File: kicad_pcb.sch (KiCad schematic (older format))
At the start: 162 parts, among them J1 USB_B_Mini, SW1 SW_Push, U1 ATmega32U4-AU, Y1 16Mhz

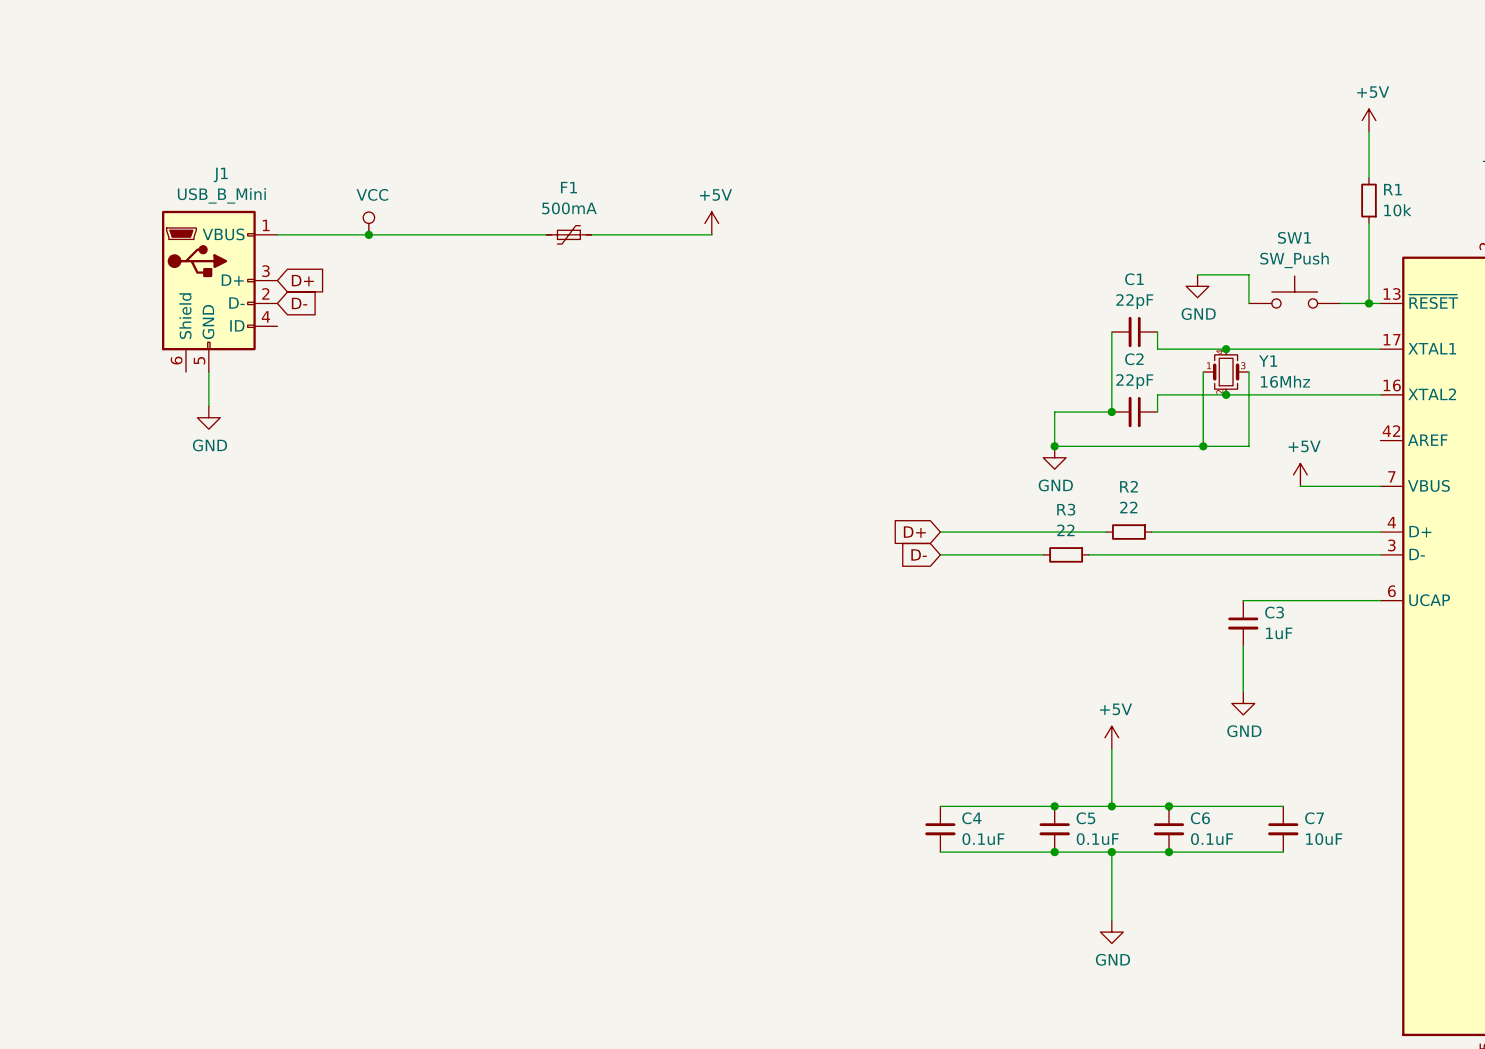
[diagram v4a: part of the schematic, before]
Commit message: Moved and re-routed traces for C7 decoupling capacitor
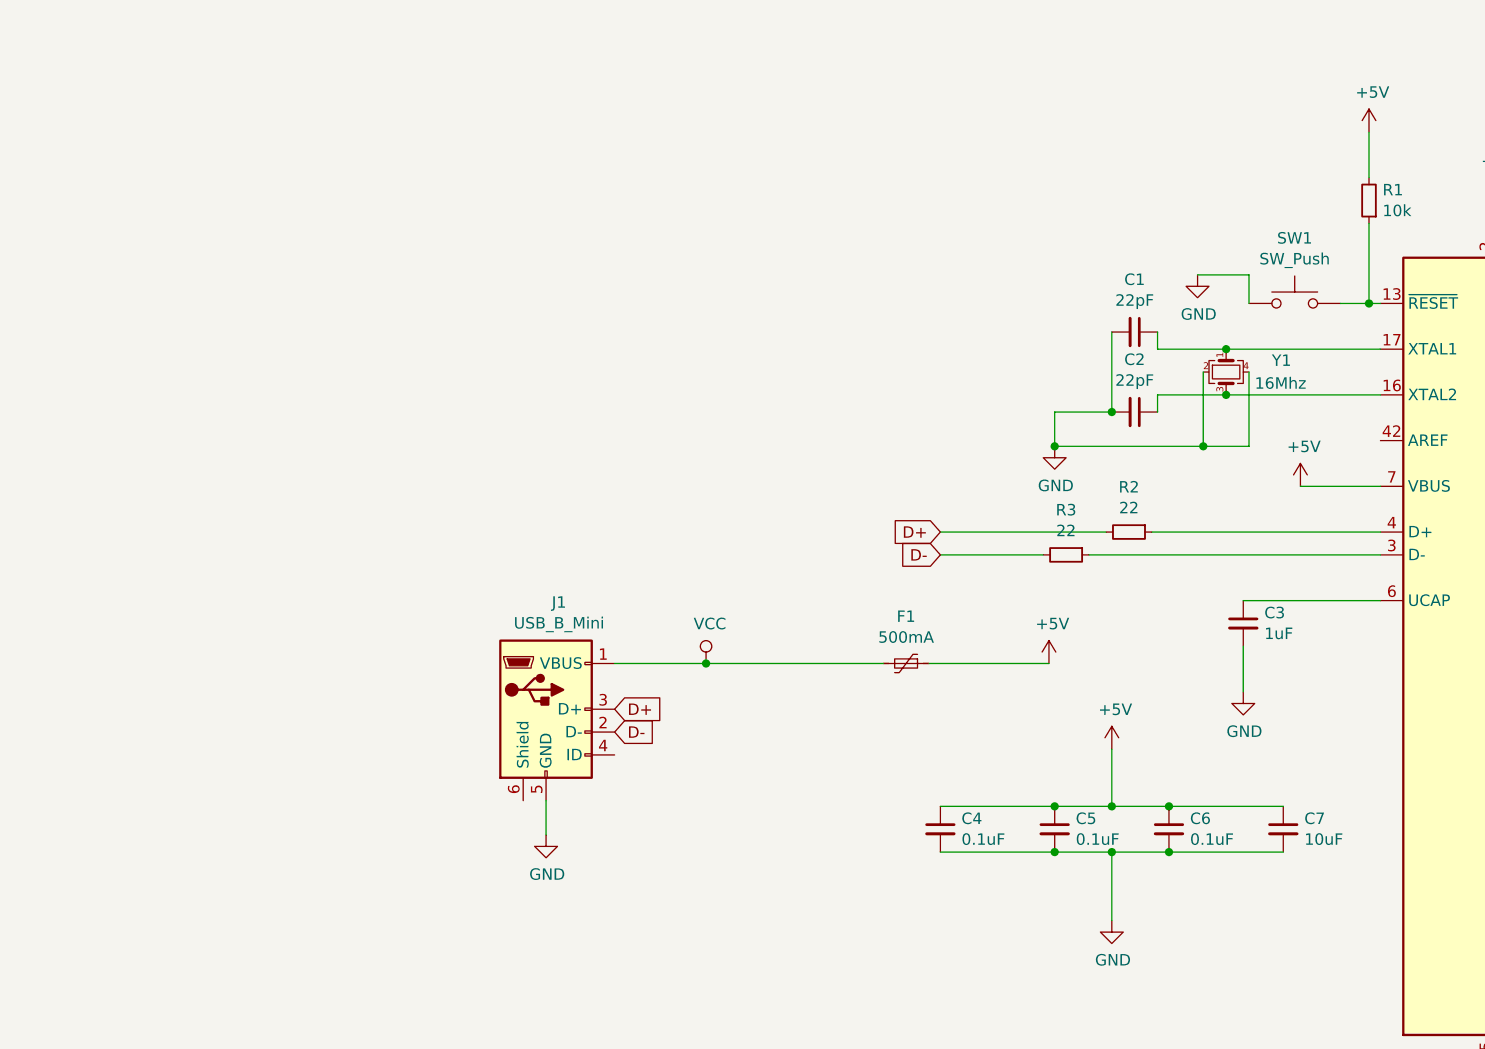
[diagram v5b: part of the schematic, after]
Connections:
- net GND: now also Y1.2, Y1.4; no longer Y1.1, Y1.3
- net at C2.1, U1.16 (XTAL2): now also Y1.3; no longer Y1.2
- net at C1.1, U1.17 (XTAL1): now also Y1.1; no longer Y1.4
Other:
- moved on the sheet: F1, J1
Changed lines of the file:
@@
 Connection ~ 6750 12500
-Wire Wire Line
-	6750 12500 7000 12500
-Connection ~ 7250 12500
-Wire Wire Line
-	7250 12500 7750 12500
 Wire Wire Line
 	7750 12700 7250 12700
@@
 Wire Wire Line
 	8175 11100 7825 11100
-$Comp
-L Device:Crystal_GND24_Small Y1
-U 1 1 5CCBDFE5
-P 7500 10600
-F 0 "Y1" H 7644 10646 50  0000 L CNN
-F 1 "16Mhz" H 7644 10555 50  0000 L CNN
-F 2 "Crystal:Crystal_SMD_3225-4Pin_3.2x2.5mm" H 7500 10600 50  0001 C CNN
-F 3 "~" H 7500 10600 50  0001 C CNN
-	1    7500 10600
-	1    0    0    -1
-$EndComp
-Wire Wire Line
-	8175 10700 7500 10700
-Wire Wire Line
-	8175 10500 7500 10500
 $Comp
 L Device:C_Small C1
@@
 $EndComp
 Wire Wire Line
-	7400 10600 7400 10925
-Wire Wire Line
 	7400 10925 6750 10925
-Wire Wire Line
-	7600 10600 7600 10925
 Wire Wire Line
 	7600 10925 7400 10925
 Connection ~ 7400 10925
 Wire Wire Line
-	7500 10700 7200 10700
-Wire Wire Line
 	7200 10700 7200 10775
-Connection ~ 7500 10700
-Wire Wire Line
-	7500 10500 7200 10500
 Wire Wire Line
 	7200 10500 7200 10425
-Connection ~ 7500 10500
 Wire Wire Line
 	7000 10425 7000 10775
@@
 L Connector:USB_B_Mini J1
 U 1 1 5CCDCA3B
-P 3050 10200
-F 0 "J1" H 3107 10667 50  0000 C CNN
-F 1 "USB_B_Mini" H 3107 10576 50  0000 C CNN
-F 2 "random-keyboard-parts:Molex-0548190589" H 3200 10150 50  0001 C CNN
-F 3 "~" H 3200 10150 50  0001 C CNN
-	1    3050 10200
+P 4525 12075
+F 0 "J1" H 4582 12542 50  0000 C CNN
+F 1 "USB_B_Mini" H 4582 12451 50  0000 C CNN
+F 2 "random-keyboard-parts:Molex-0548190589" H 4675 12025 50  0001 C CNN
+F 3 "~" H 4675 12025 50  0001 C CNN
+	1    4525 12075
 	1    0    0    -1
 $EndComp
@@
 L Device:Polyfuse_Small F1
 U 1 1 5CCDD8D1
-P 4625 10000
-F 0 "F1" V 4420 10000 50  0000 C CNN
-F 1 "500mA" V 4511 10000 50  0000 C CNN
-F 2 "Fuse:Fuse_1206_3216Metric" H 4675 9800 50  0001 L CNN
-F 3 "~" H 4625 10000 50  0001 C CNN
-	1    4625 10000
+P 6100 11875
+F 0 "F1" V 5895 11875 50  0000 C CNN
+F 1 "500mA" V 5986 11875 50  0000 C CNN
+F 2 "Fuse:Fuse_1206_3216Metric" H 6150 11675 50  0001 L CNN
+F 3 "~" H 6100 11875 50  0001 C CNN
+	1    6100 11875
 	0    1    1    0
 $EndComp
@@
 L power:+5V #PWR0111
 U 1 1 5CCDE608
-P 5250 10000
-F 0 "#PWR0111" H 5250 9850 50  0001 C CNN
-F 1 "+5V" H 5265 10173 50  0000 C CNN
-F 2 "" H 5250 10000 50  0001 C CNN
-F 3 "" H 5250 10000 50  0001 C CNN
-	1    5250 10000
+P 6725 11875
+F 0 "#PWR0111" H 6725 11725 50  0001 C CNN
+F 1 "+5V" H 6740 12048 50  0000 C CNN
+F 2 "" H 6725 11875 50  0001 C CNN
+F 3 "" H 6725 11875 50  0001 C CNN
+	1    6725 11875
 	1    0    0    -1
 $EndComp
@@
 L power:VCC #PWR0112
 U 1 1 5CCDEDD0
-P 3750 10000
-F 0 "#PWR0112" H 3750 9850 50  0001 C CNN
-F 1 "VCC" H 3767 10173 50  0000 C CNN
-F 2 "" H 3750 10000 50  0001 C CNN
-F 3 "" H 3750 10000 50  0001 C CNN
-	1    3750 10000
-	1    0    0    -1
-$EndComp
-Wire Wire Line
-	3350 10000 3750 10000
-Connection ~ 3750 10000
-Wire Wire Line
-	3750 10000 4525 10000
-Wire Wire Line
-	4725 10000 5250 10000
-Text GLabel 3350 10200 2    50   Input ~ 0
+P 5225 11875
+F 0 "#PWR0112" H 5225 11725 50  0001 C CNN
+F 1 "VCC" H 5242 12048 50  0000 C CNN
+F 2 "" H 5225 11875 50  0001 C CNN
+F 3 "" H 5225 11875 50  0001 C CNN
+	1    5225 11875
+	1    0    0    -1
+$EndComp
+Wire Wire Line
+	4825 11875 5225 11875
+Connection ~ 5225 11875
+Wire Wire Line
+	5225 11875 6000 11875
+Wire Wire Line
+	6200 11875 6725 11875
+Text GLabel 4825 12075 2    50   Input ~ 0
 D+
-Text GLabel 3350 10300 2    50   Input ~ 0
+Text GLabel 4825 12175 2    50   Input ~ 0
 D-
 $Comp
 L power:GND #PWR0113
 U 1 1 5CCE29A1
-P 3050 10750
-F 0 "#PWR0113" H 3050 10500 50  0001 C CNN
-F 1 "GND" H 3055 10577 50  0000 C CNN
-F 2 "" H 3050 10750 50  0001 C CNN
-F 3 "" H 3050 10750 50  0001 C CNN
-	1    3050 10750
-	1    0    0    -1
-$EndComp
-Wire Wire Line
-	3050 10600 3050 10750
+P 4525 12625
+F 0 "#PWR0113" H 4525 12375 50  0001 C CNN
+F 1 "GND" H 4530 12452 50  0000 C CNN
+F 2 "" H 4525 12625 50  0001 C CNN
+F 3 "" H 4525 12625 50  0001 C CNN
+	1    4525 12625
+	1    0    0    -1
+$EndComp
+Wire Wire Line
+	4525 12475 4525 12625
 Wire Wire Line
 	7500 5050 7500 6050
@@
 Text GLabel 9475 11500 2    50   Input ~ 0
 ROW1
+Wire Wire Line
+	6750 12500 7000 12500
+Connection ~ 7250 12500
+Wire Wire Line
+	7250 12500 7750 12500
+Connection ~ 7500 10500
+Wire Wire Line
+	7500 10500 7200 10500
+Wire Wire Line
+	8175 10500 7500 10500
+Wire Wire Line
+	7600 10600 7600 10925
+Connection ~ 7500 10700
+Wire Wire Line
+	7500 10700 7200 10700
+Wire Wire Line
+	8175 10700 7500 10700
+Wire Wire Line
+	7400 10600 7400 10925
+$Comp
+L Device:Crystal_GND24_Small Y1
+U 1 1 5CCBDFE5
+P 7500 10600
+F 0 "Y1" V 7450 10800 50  0000 L CNN
+F 1 "16Mhz" V 7550 10725 50  0000 L CNN
+F 2 "Crystal:Crystal_SMD_3225-4Pin_3.2x2.5mm" H 7500 10600 50  0001 C CNN
+F 3 "~" H 7500 10600 50  0001 C CNN
+	1    7500 10600
+	0    1    1    0
+$EndComp
 $EndSCHEMATC

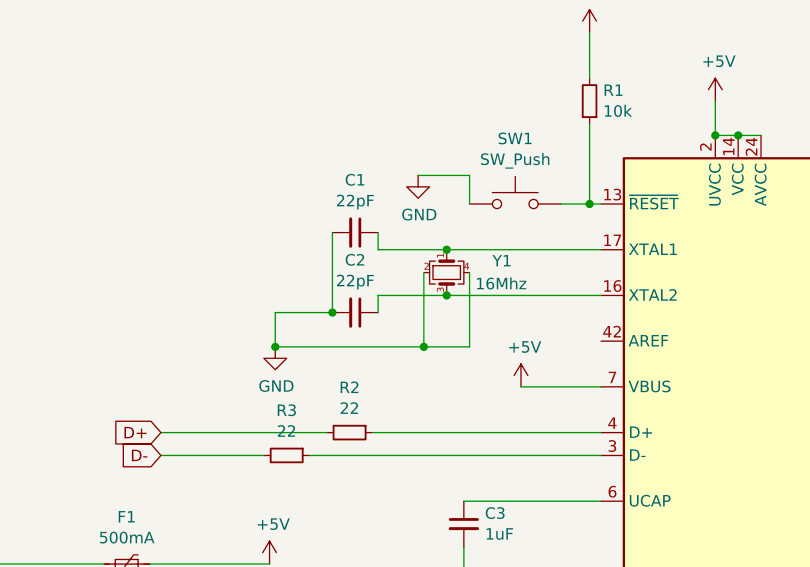
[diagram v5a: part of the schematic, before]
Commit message: started to restructure the routing
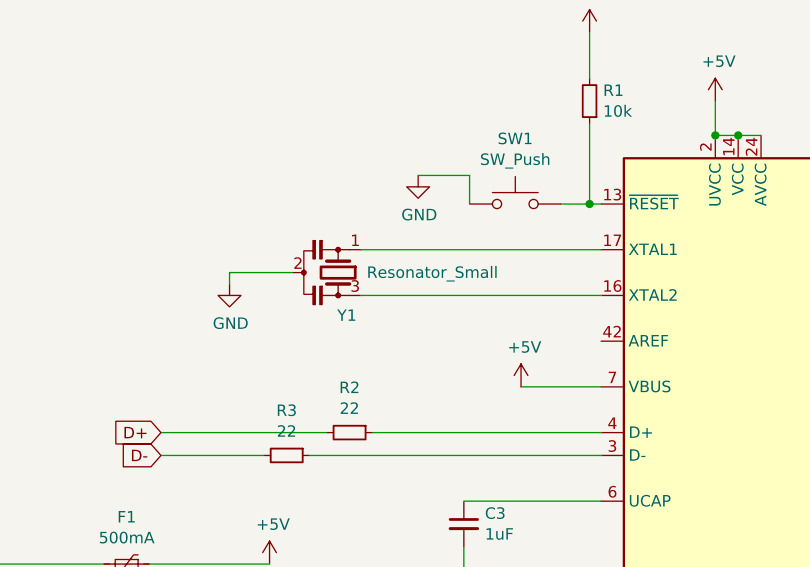
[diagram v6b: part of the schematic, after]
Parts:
- removed C1, C2: 22pF, Capacitor_SMD:C_0805_2012Metric, symbol Device:C_Small
- removed Y1: 16Mhz, Crystal:Crystal_SMD_3225-4Pin_3.2x2.5mm, symbol Device:Crystal_GND24_Small
- added Y1: Resonator_Small, Crystal:Resonator_SMD_muRata_CSTxExxV-3Pin_3.0x1.1mm, symbol Device:Resonator_Small
- J1: footprint random-keyboard-parts:Molex-0548190589 -> random-keyboard-parts:Molex-0548190519
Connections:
- net GND: now also Y1.2
- net at U1.16 (XTAL2): now also Y1.3
- net at U1.17 (XTAL1): now also Y1.1
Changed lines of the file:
@@
 	8175 11100 7825 11100
-$Comp
-L Device:C_Small C1
-U 1 1 5CCC2436
-P 7100 10425
-F 0 "C1" V 6871 10425 50  0000 C CNN
-F 1 "22pF" V 6962 10425 50  0000 C CNN
-F 2 "Capacitor_SMD:C_0805_2012Metric" H 7100 10425 50  0001 C CNN
-F 3 "~" H 7100 10425 50  0001 C CNN
-	1    7100 10425
-	0    1    1    0
-$EndComp
-$Comp
-L Device:C_Small C2
-U 1 1 5CCC3005
-P 7100 10775
-F 0 "C2" V 6871 10775 50  0000 C CNN
-F 1 "22pF" V 6962 10775 50  0000 C CNN
-F 2 "Capacitor_SMD:C_0805_2012Metric" H 7100 10775 50  0001 C CNN
-F 3 "~" H 7100 10775 50  0001 C CNN
-	1    7100 10775
-	0    1    1    0
-$EndComp
-$Comp
-L power:GND #PWR0108
-U 1 1 5CCC33BA
-P 6750 10925
-F 0 "#PWR0108" H 6750 10675 50  0001 C CNN
-F 1 "GND" H 6755 10752 50  0000 C CNN
-F 2 "" H 6750 10925 50  0001 C CNN
-F 3 "" H 6750 10925 50  0001 C CNN
-	1    6750 10925
-	1    0    0    -1
-$EndComp
-Wire Wire Line
-	7400 10925 6750 10925
-Wire Wire Line
-	7600 10925 7400 10925
-Connection ~ 7400 10925
-Wire Wire Line
-	7200 10700 7200 10775
-Wire Wire Line
-	7200 10500 7200 10425
-Wire Wire Line
-	7000 10425 7000 10775
-Wire Wire Line
-	7000 10775 6750 10775
-Wire Wire Line
-	6750 10775 6750 10925
-Connection ~ 7000 10775
-Connection ~ 6750 10925
 $Comp
 L Switch:SW_Push SW1
@@
 F 0 "J1" H 4582 12542 50  0000 C CNN
 F 1 "USB_B_Mini" H 4582 12451 50  0000 C CNN
-F 2 "random-keyboard-parts:Molex-0548190589" H 4675 12025 50  0001 C CNN
+F 2 "random-keyboard-parts:Molex-0548190519" H 4675 12025 50  0001 C CNN
 F 3 "~" H 4675 12025 50  0001 C CNN
 	1    4525 12075
@@
 Wire Wire Line
 	7250 12500 7750 12500
-Connection ~ 7500 10500
-Wire Wire Line
-	7500 10500 7200 10500
-Wire Wire Line
-	8175 10500 7500 10500
-Wire Wire Line
-	7600 10600 7600 10925
-Connection ~ 7500 10700
-Wire Wire Line
-	7500 10700 7200 10700
-Wire Wire Line
-	8175 10700 7500 10700
-Wire Wire Line
-	7400 10600 7400 10925
-$Comp
-L Device:Crystal_GND24_Small Y1
-U 1 1 5CCBDFE5
-P 7500 10600
-F 0 "Y1" V 7450 10800 50  0000 L CNN
-F 1 "16Mhz" V 7550 10725 50  0000 L CNN
-F 2 "Crystal:Crystal_SMD_3225-4Pin_3.2x2.5mm" H 7500 10600 50  0001 C CNN
-F 3 "~" H 7500 10600 50  0001 C CNN
-	1    7500 10600
+$Comp
+L Device:Resonator_Small Y1
+U 1 1 5D4D1439
+P 7025 10600
+F 0 "Y1" V 7213 10596 50  0000 L CNN
+F 1 "Resonator_Small" V 7025 10725 50  0000 L CNN
+F 2 "Crystal:Resonator_SMD_muRata_CSTxExxV-3Pin_3.0x1.1mm" H 7000 10600 50  0001 C CNN
+F 3 "~" H 7000 10600 50  0001 C CNN
+	1    7025 10600
 	0    1    1    0
 $EndComp
+$Comp
+L power:GND #PWR0108
+U 1 1 5CCC33BA
+P 6550 10650
+F 0 "#PWR0108" H 6550 10400 50  0001 C CNN
+F 1 "GND" H 6555 10477 50  0000 C CNN
+F 2 "" H 6550 10650 50  0001 C CNN
+F 3 "" H 6550 10650 50  0001 C CNN
+	1    6550 10650
+	1    0    0    -1
+$EndComp
+Wire Wire Line
+	8175 10500 7125 10500
+Wire Wire Line
+	7125 10700 8175 10700
+Wire Wire Line
+	6825 10600 6550 10600
+Wire Wire Line
+	6550 10600 6550 10650
 $EndSCHEMATC

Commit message: further routing
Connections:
- net COL0: now also U1.41 (PF0); no longer U1.1 (PE6)
- net COL1: now also U1.40 (PF1); no longer U1.41 (PF0)
- net COL10: now also U1.28 (PB4); no longer U1.25 (PD4)
- net COL11: now also U1.21 (PD3); no longer U1.22 (PD5)
- net COL12: now also U1.20 (PD2); no longer U1.21 (PD3)
- net COL13: now also U1.19 (PD1); no longer U1.20 (PD2)
- net COL14: now also U1.18 (PD0); no longer U1.19 (PD1)
- net COL2: now also U1.39 (PF4); no longer U1.40 (PF1)
- net COL3: now also U1.38 (PF5); no longer U1.39 (PF4)
- net COL6: now also U1.32 (PC7); no longer U1.38 (PF5)
- net COL8: now also U1.30 (PB6); no longer U1.28 (PB4)
- net COL9: now also U1.29 (PB5); no longer U1.26 (PD6)
- net ROW1: now also U1.1 (PE6); no longer U1.18 (PD0)
- net ROW2: now also U1.22 (PD5); no longer U1.29 (PB5)
- net ROW3: now also U1.25 (PD4); no longer U1.12 (PB7)
- net ROW4: now also U1.26 (PD6); no longer U1.30 (PB6)
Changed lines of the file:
@@
 	5000 5050 5000 6050
 Connection ~ 5000 5050
-Text GLabel 9475 10800 2    50   Input ~ 0
+Text GLabel 9475 12000 2    50   Input ~ 0
 ROW2
 Text GLabel 9475 10300 2    50   Input ~ 0
 ROW0
-Text GLabel 9475 11800 2    50   Input ~ 0
+Text GLabel 9475 11700 2    50   Input ~ 0
 COL12
-Text GLabel 9475 11700 2    50   Input ~ 0
+Text GLabel 9475 11600 2    50   Input ~ 0
 COL13
-Text GLabel 9475 11900 2    50   Input ~ 0
+Text GLabel 9475 10700 2    50   Input ~ 0
 COL10
 Text GLabel 9475 13100 2    50   Input ~ 0
@@
 Text GLabel 9475 13200 2    50   Input ~ 0
 COL5
+Text GLabel 9475 13000 2    50   Input ~ 0
+COL3
 Text GLabel 9475 12900 2    50   Input ~ 0
-COL3
-Text GLabel 9475 12500 2    50   Input ~ 0
-COL0
+COL2
 Text GLabel 9475 12800 2    50   Input ~ 0
-COL2
-Text GLabel 9475 12700 2    50   Input ~ 0
 COL1
 Connection ~ 8675 13600
@@
 	1    0    0    -1
 $EndComp
-Text GLabel 9475 11600 2    50   Input ~ 0
+Text GLabel 9475 11500 2    50   Input ~ 0
 COL14
 Wire Wire Line
@@
 Wire Wire Line
 	9475 11600 9375 11600
-Text GLabel 9475 13000 2    50   Input ~ 0
+Text GLabel 9475 11300 2    50   Input ~ 0
 COL6
-Text GLabel 9475 10700 2    50   Input ~ 0
+Text GLabel 9475 10900 2    50   Input ~ 0
 COL8
 Wire Wire Line
@@
 Wire Wire Line
 	9475 13200 9375 13200
-Text GLabel 9475 10900 2    50   Input ~ 0
+Text GLabel 9475 12100 2    50   Input ~ 0
 ROW4
-Text GLabel 9475 11000 2    50   Input ~ 0
+Text GLabel 9475 11900 2    50   Input ~ 0
 ROW3
-Text GLabel 9475 12100 2    50   Input ~ 0
+Text GLabel 9475 10800 2    50   Input ~ 0
 COL9
-Text GLabel 9475 12000 2    50   Input ~ 0
+Text GLabel 9475 11800 2    50   Input ~ 0
 COL11
 Text GLabel 9475 11200 2    50   Input ~ 0
 COL7
-Text GLabel 9475 11500 2    50   Input ~ 0
+Text GLabel 9475 12500 2    50   Input ~ 0
 ROW1
 Wire Wire Line
@@
 Wire Wire Line
 	6550 10600 6550 10650
+Text GLabel 9475 12700 2    50   Input ~ 0
+COL0
 $EndSCHEMATC

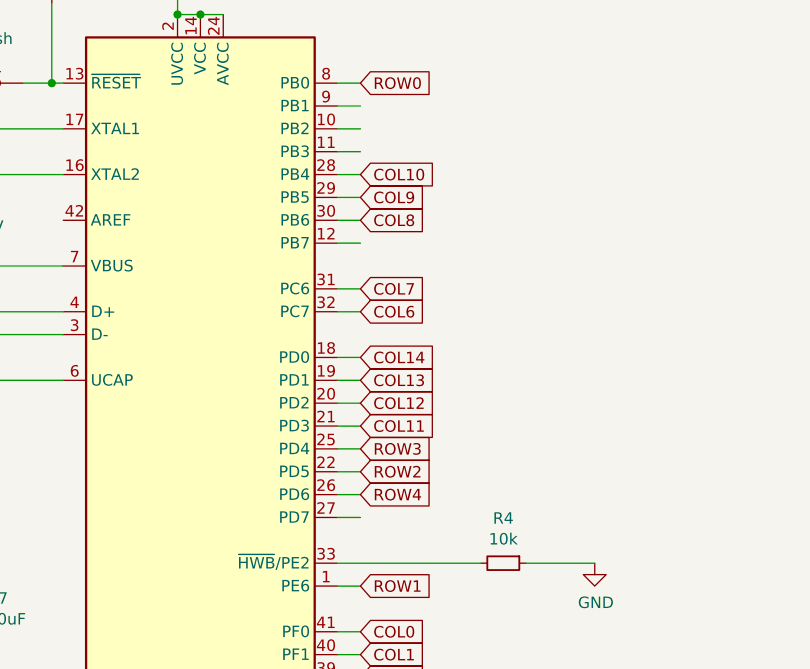
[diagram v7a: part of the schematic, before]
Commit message: finished all routing, except the bottom row
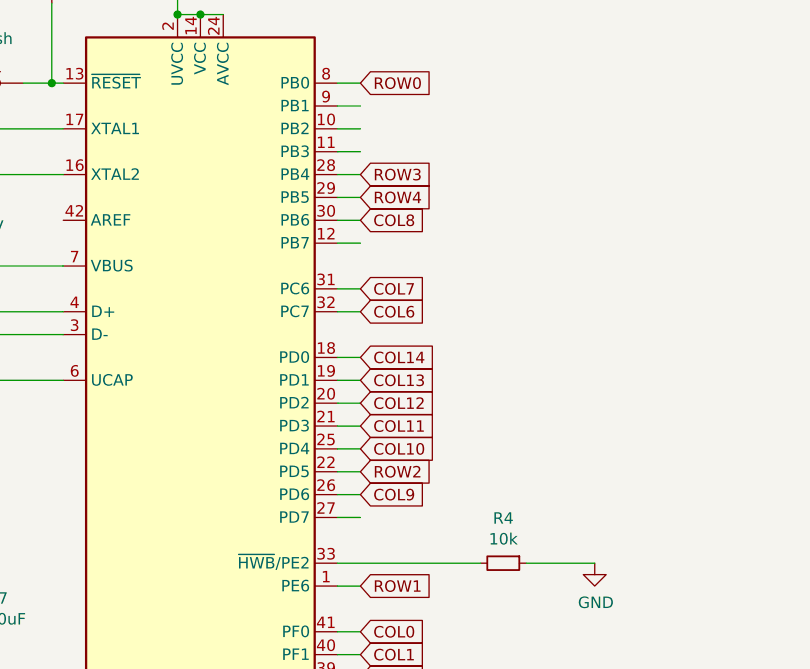
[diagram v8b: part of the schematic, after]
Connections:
- net COL10: now also U1.25 (PD4); no longer U1.28 (PB4)
- net COL9: now also U1.26 (PD6); no longer U1.29 (PB5)
- net ROW3: now also U1.28 (PB4); no longer U1.25 (PD4)
- net ROW4: now also U1.29 (PB5); no longer U1.26 (PD6)
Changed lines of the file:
@@
 Text GLabel 9475 11600 2    50   Input ~ 0
 COL13
-Text GLabel 9475 10700 2    50   Input ~ 0
+Text GLabel 9475 11900 2    50   Input ~ 0
 COL10
 Text GLabel 9475 13100 2    50   Input ~ 0
@@
 Wire Wire Line
 	9475 13200 9375 13200
+Text GLabel 9475 10800 2    50   Input ~ 0
+ROW4
+Text GLabel 9475 10700 2    50   Input ~ 0
+ROW3
 Text GLabel 9475 12100 2    50   Input ~ 0
-ROW4
-Text GLabel 9475 11900 2    50   Input ~ 0
-ROW3
-Text GLabel 9475 10800 2    50   Input ~ 0
 COL9
 Text GLabel 9475 11800 2    50   Input ~ 0
